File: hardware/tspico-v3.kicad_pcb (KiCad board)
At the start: 4 copper layers, 130 x 64 mm, 157 parts, among them J1 USB-C, J2 microSD, J3 OLED 1.27in 128x96, J4 3.5mm stereo, J5 Joystick, P1 TS2068_Edge, SW1 TS Reset, SW2 NMI, SW3 RUN, SW4 BOOTSEL, U1 74LVC245APW, U10 74LVC257APW, U11 74LVC257APW, U12 74LVC574APW, U13 74LVC574APW, U14 74HC273PW, U15 74LVC541APW, U16 74LVC139PW, U2 74LVC245APW, U20 RP2350B, U21 W25Q128JVSIQ, U22 APS6404L-3SQR-SN, U3 74LVC245APW, U30 TLV1117LV33, U31 TLV1117LV33, U4 74LVC245APW, U40 ESP32-C3-WROOM-02-N4, U5 74LVC04APW, U50 MCP6002, U6 74LVC08APW, U7 74LVC06APW, U8 74LVC126APW, U9 74LVC1G86, Y1 12MHz

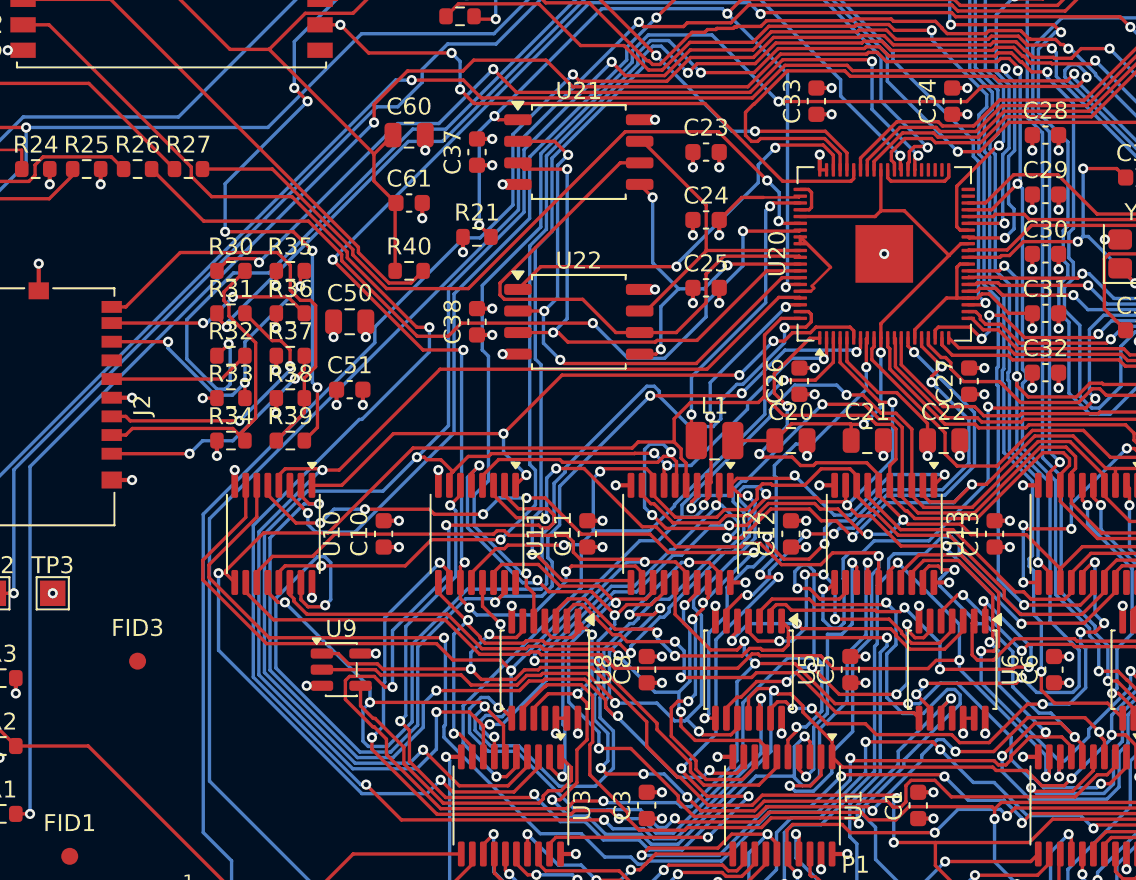
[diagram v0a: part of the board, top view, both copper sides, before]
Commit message: Hand-finish the last eight connections: fully routed, zero DRC errors
finish_route.py adds plane vias, clearance-checked stubs and single-layer
A* routing. Five signals run partly on the +3V3 plane layer (In2). SD_MISO
moves from GP36 to GP32 (both SPI0 RX) because the GP36 pad has no exit.
Schematic, GPIO table and README updated.

Co-Authored-By: Claude Fable 5.1 <noreply@anthropic.com>
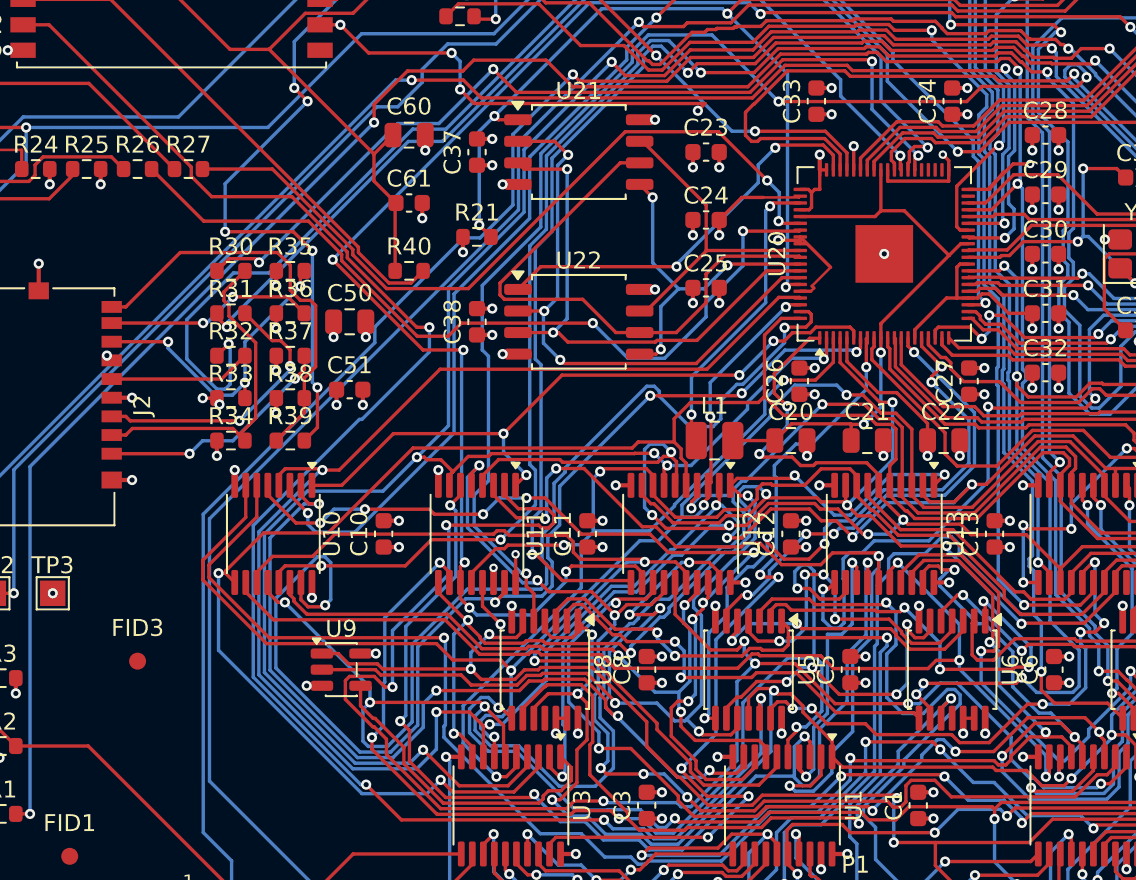
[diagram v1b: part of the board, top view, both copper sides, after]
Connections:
- U20 pad 40: unconnected-(U20-GPIO32-Pad40) -> SD_MISO
- U20 pad 45: SD_MISO -> (no net)
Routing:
- net SD_MISO: track 0.84 -> 64.7 mm, vias 1 -> 3
- net nMWR: track 64.4 -> 90.2 mm
- net MA14: track 19.8 -> 44.8 mm
- net +3V3: track 99.1 -> 105.1 mm, vias 69 -> 72
- net WIFI_TX: track 36.8 -> 37.6 mm, vias 3 -> 5
- net GND: track 123.8 -> 124.2 mm, vias 116 -> 117
- net MA6: track 59.3 -> 59.2 mm, vias 5 -> 6

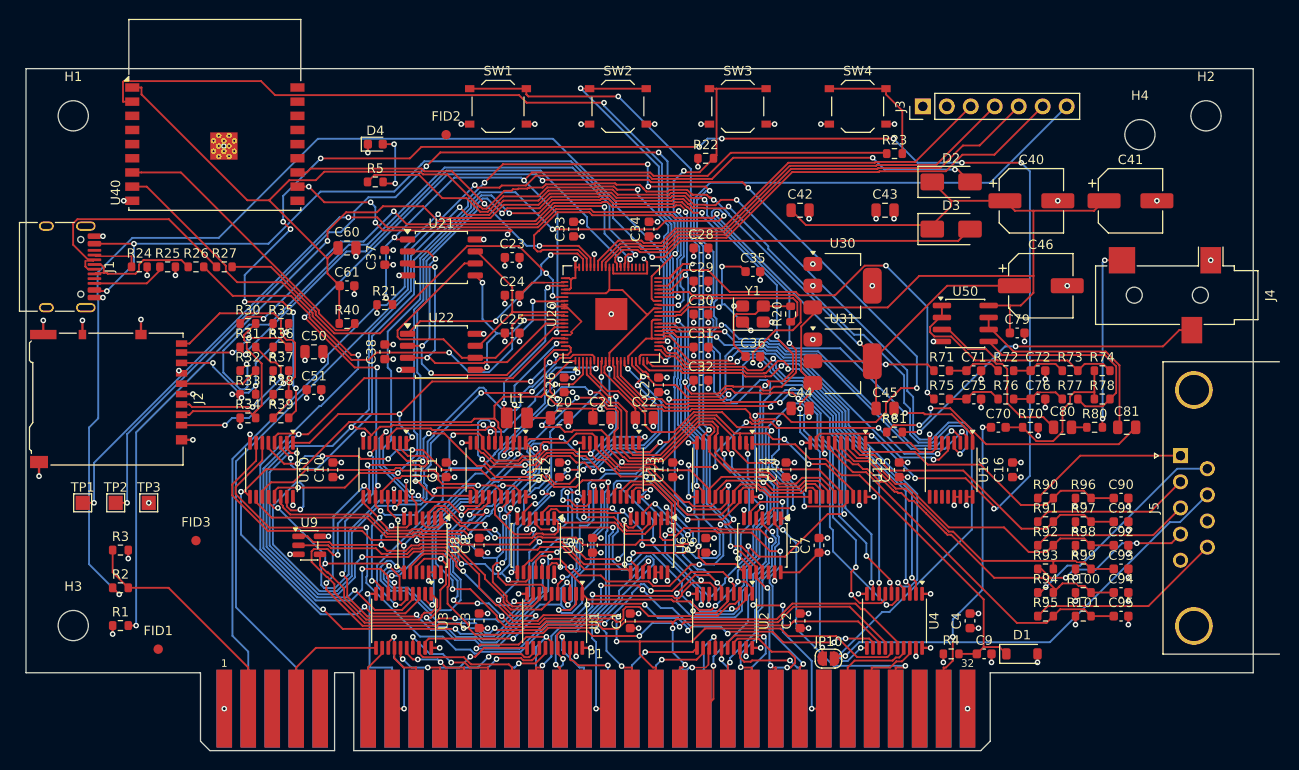
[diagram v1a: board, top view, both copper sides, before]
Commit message: Relayout: 130 x 64.25 mm board with the consolidated logic and cheaper BOM
Regulator and crystal hand-routed per the RP2350 design guide (locked
pre-routes), TF-01A socket flush with the edge, custom footprints from LCSC
land patterns, 0.15 mm signal tracks, 0.6/0.3 vias throughout. New flow:
gen_layout -> preroute -> autoroute -> finish. Zero DRC violations; open are
two nets of the unfitted DMA option (nMRD, nWR_ALO). Fab outputs regenerated.

Co-Authored-By: Claude Fable 5.1 <noreply@anthropic.com>
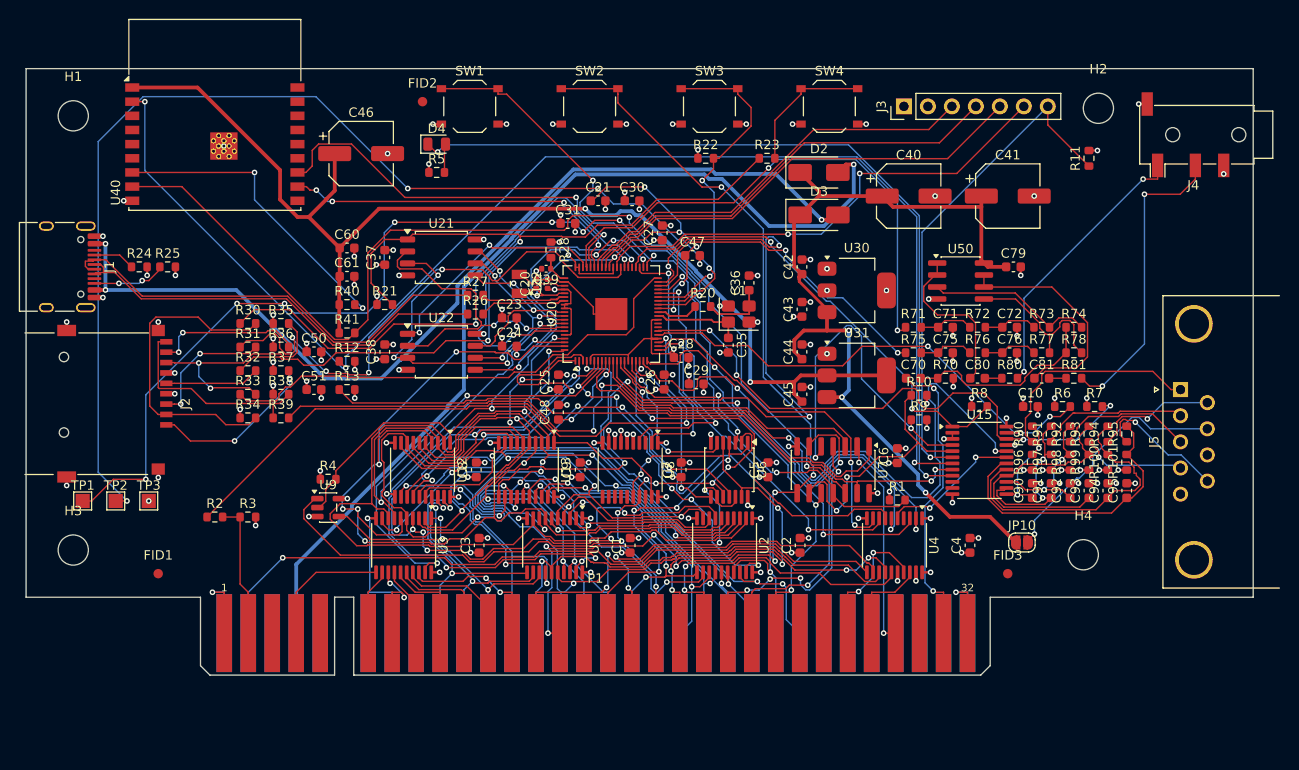
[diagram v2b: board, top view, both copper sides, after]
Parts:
- removed C11, C12, C13, C14, C15, C16, C32, C33, C34: 100n, C_0603_1608Metric
- removed D1: B5819W, D_SOD-123
- removed U10, U11: 74LVC257APW, TSSOP-16_4.4x5mm_P0.65mm
- removed U14: 74HC273PW, TSSOP-20_4.4x6.5mm_P0.65mm
- removed U16: 74LVC139PW, TSSOP-16_4.4x5mm_P0.65mm
- removed U5: 74LVC04APW, TSSOP-14_4.4x5mm_P0.65mm
- added C39: 4.7u, C_0402_1005Metric, F.Cu at (55.1, 21.2)
- added C47: 100n, C_0603_1608Metric, F.Cu at (70.6, 19.8)
- added C48: 100n, C_0603_1608Metric, F.Cu at (56.4, 36.4)
- added R10: 10k, R_0603_1608Metric, F.Cu at (94.6, 34.6)
- added R11: 10k, R_0603_1608Metric, F.Cu at (112.6, 9.50)
- added R12: 10k, R_0603_1608Metric, F.Cu at (34.0, 31.0)
- added R13: 10k, R_0603_1608Metric, F.Cu at (34.0, 34.0)
- added R28: 33, R_0603_1608Metric, F.Cu at (55.6, 19.2)
- added R41: 10k, R_0603_1608Metric, F.Cu at (34.0, 28.0)
- added R6: 4k7, R_0603_1608Metric, F.Cu at (109.8, 35.8)
- added R7: 4k7, R_0603_1608Metric, F.Cu at (113.2, 35.8)
- added R8: 10k, R_0603_1608Metric, F.Cu at (101.0, 35.8)
- added R9: 10k, R_0603_1608Metric, F.Cu at (94.6, 37.2)
- C20, C22: footprint C_0805_2012Metric -> C_0402_1005Metric
- C21: value 4.7u -> 100n; footprint C_0805_2012Metric -> C_0603_1608Metric
- C40, C41, C46: footprint CP_Elec_6.3x5.9 -> CP_Elec_6.3x5.4
- C42, C43, C44, C45, C50, C60, C80, C81: footprint C_0805_2012Metric -> C_0603_1608Metric
- C9: value 1u -> 100n
- D4: footprint LED_0603_1608Metric -> LED_0805_2012Metric
- J2: footprint microSD_HC_Hirose_DM3AT-SF-PEJM5 -> microSD_TF-01A
- J4: footprint Jack_3.5mm_CUI_SJ-3523-SMT_Horizontal -> Jack_3.5mm_PJ320D_Horizontal
- L1: footprint L_1008_2520Metric -> L_Abracon_AOTA-B201610
- R5: value 1k -> 100
- U15: value 74LVC541APW -> XL9555; footprint TSSOP-20_4.4x6.5mm_P0.65mm -> TSSOP-24_4.4x7.8mm_P0.65mm
- U21: value W25Q128JVSIQ -> GD25Q128ESIGR
- U6: value 74LVC08APW -> 74LVC32APW
- U7: value 74LVC06APW -> 74LVC06AD; footprint TSSOP-14_4.4x5mm_P0.65mm -> SOIC-14_3.9x8.7mm_P1.27mm
- U8: value 74LVC126APW -> 74LVC245APW; footprint TSSOP-14_4.4x5mm_P0.65mm -> TSSOP-20_4.4x6.5mm_P0.65mm
- moved FID3 86.1 mm to (104.0, 53.5)
- moved R1 83.4 mm to (92.3, 45.7)
- moved C10 74.2 mm to (106.4, 35.8), turned to 0 degrees
- moved C46 73.3 mm to (35.5, 9.00)
- moved R4 68.5 mm to (32.0, 43.5)
- moved C9 47.0 mm to (58.7, 42.5), turned to 90 degrees
- moved H4 44.9 mm to (112.0, 51.5)
- moved R26 30.0 mm to (47.6, 26.0)
- moved R27 26.8 mm to (47.6, 24.0)
- moved JP10 23.9 mm to (105.5, 50.2)
- moved U8 23.4 mm to (64.0, 42.5)
- moved C21 23.0 mm to (60.6, 14.0)
- moved C6 22.4 mm to (92.3, 41.0)
- moved R95 21.1 mm to (116.6, 38.7), turned to 90 degrees
- moved C5 20.2 mm to (78.6, 42.5)
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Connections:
- net /Local Bus and Registers/LED_K renamed /Local Bus and Registers/LED_A
- C9 pad 1: /Local Bus and Registers/nPOR -> +3V3
- D4 pad 1: GND -> /Local Bus and Registers/nLED
- P1 pad A25: /2068 Interface/nM1 -> unconnected-(P1-~{M1}-PadA25)
- P1 pad A26: /2068 Interface/nRFSH -> unconnected-(P1-~{RFSH}-PadA26)
- R4 pad 2: /Local Bus and Registers/nPOR -> nDMA_EN
- R5 pad 1: LED -> +3V3
- U1 pad 1: DMA_EN -> GND
- U1 pad 19: GND -> nAEN_X
- U1 pad 2: MA12 -> MD4
- U1 pad 3: MA13 -> MD5
- U1 pad 4: MA14 -> MD6
- U1 pad 5: MA15 -> MD7
- U1 pad 6: MA3 -> MD3
- U1 pad 7: MA2 -> MD2
- U1 pad 8: MA1 -> MD1
- U1 pad 9: MA0 -> MD0
- U12 pad 11: /Local Bus and Registers/nWR_ALO -> nWR_ALO
- U12 pad 12: MA7 -> /2068 Interface/A7
- U12 pad 13: MA6 -> /2068 Interface/A6
- U12 pad 14: MA5 -> /2068 Interface/A5
- U12 pad 15: MA4 -> /2068 Interface/A4
- U12 pad 16: MA3 -> /2068 Interface/A3
- U12 pad 17: MA2 -> /2068 Interface/A2
- U12 pad 18: MA1 -> /2068 Interface/A1
- U12 pad 19: MA0 -> /2068 Interface/A0
- U13 pad 11: /Local Bus and Registers/nWR_AHI -> nWR_AHI
- U13 pad 12: MA15 -> /2068 Interface/A15
- U13 pad 13: MA14 -> /2068 Interface/A14
- U13 pad 14: MA13 -> /2068 Interface/A13
- U13 pad 15: MA12 -> /2068 Interface/A12
- U13 pad 16: MA11 -> /2068 Interface/A11
- U13 pad 17: MA10 -> /2068 Interface/A10
- U13 pad 18: MA9 -> /2068 Interface/A9
- U13 pad 19: MA8 -> /2068 Interface/A8
- U15 pad 1: /Local Bus and Registers/nRD_STAT -> nIOX_INT
- U15 pad 10: GND -> unconnected-(U15-IO0_6-Pad10)
- U15 pad 11: MD7 -> unconnected-(U15-IO0_7-Pad11)
- U15 pad 12: MD6 -> GND
- U15 pad 13: MD5 -> JOY_UP
- U15 pad 14: MD4 -> JOY_DOWN
- U15 pad 15: MD3 -> JOY_LEFT
- U15 pad 16: MD2 -> JOY_RIGHT
- U15 pad 17: MD1 -> JOY_FIRE1
- U15 pad 18: MD0 -> JOY_FIRE2
- U15 pad 19: GND -> nBUSAK_L
- U15 pad 2: JOY_UP -> GND
- U15 pad 20: +3V3 -> SD_CD
- U15 pad 3: JOY_DOWN -> GND
- U15 pad 4: JOY_LEFT -> BUSRQ
- U15 pad 5: JOY_RIGHT -> NMI_REQ
- U15 pad 6: JOY_FIRE1 -> nOLED_RST
- U15 pad 7: JOY_FIRE2 -> WIFI_EN
- U15 pad 8: nBUSAK -> WIFI_DL
- U15 pad 9: SD_CD -> /Local Bus and Registers/nLED
- U2 pad 1: DMA_EN -> GND
- U2 pad 19: GND -> nAEN_Y
- U2 pad 2: MA4 -> MD0
- U2 pad 3: MA5 -> MD1
- U2 pad 4: MA6 -> MD2
- U2 pad 5: MA7 -> MD3
- U2 pad 6: MA8 -> MD4
- U2 pad 7: MA9 -> MD5
- U2 pad 8: MA10 -> MD6
- U2 pad 9: MA11 -> MD7
- U20 pad 14: nMREQ_V -> nMEMRD
- U20 pad 16: nIORQ_V -> nMEMWR
- U20 pad 17: nRD_L -> nIORD
- U20 pad 18: nWR_L -> nIOWR
- U20 pad 25: REG_SEL0 -> I2C_SDA
- U20 pad 26: REG_SEL1 -> I2C_SCL
- U20 pad 27: nREG_STB -> nWR_ALO
- U20 pad 39: unconnected-(U20-GPIO31-Pad39) -> nWR_AHI
- U20 pad 42: unconnected-(U20-GPIO33-Pad42) -> nDMA_EN
- U20 pad 43: unconnected-(U20-GPIO34-Pad43) -> nDMA_MREQ
- U20 pad 44: unconnected-(U20-GPIO35-Pad44) -> nIOX_INT
- U20 pad 45: (no net) -> unconnected-(U20-GPIO36-Pad45)
- U20 pad 6: ASEL -> nAEN_X
- U20 pad 61: +3V3 -> /RP2350B Core/VREG_AVDD
- U20 pad 7: nAOE -> nAEN_Y
- U4 pad 15: /2068 Interface/nRD -> nBUSAK
- U4 pad 16: /2068 Interface/nWR -> GND
- U4 pad 4: nWR_L -> unconnected-(U4-A2-Pad4)
- U4 pad 5: nRD_L -> nBUSAK_L
- U6 pad 1: /2068 Interface/MREQ_H -> /2068 Interface/nMREQ
- U6 pad 10: nMWR -> /2068 Interface/nRD
- U6 pad 11: unconnected-(U6-Pad11) -> nIOWR
- U6 pad 12: GND -> /2068 Interface/nIORQ
- U6 pad 13: GND -> /2068 Interface/nWR
- U6 pad 2: /2068 Interface/nRFSH -> /2068 Interface/nRD
- U6 pad 3: /2068 Interface/MREQ_RFSH -> nMEMRD
- U6 pad 4: /2068 Interface/IORQ_H -> /2068 Interface/nMREQ
- U6 pad 5: /2068 Interface/nM1 -> /2068 Interface/nWR
- U6 pad 6: /2068 Interface/IORQ_M1 -> nMEMWR
- U6 pad 8: /2068 Interface/nDMA_MREQ -> nIORD
- U6 pad 9: nMRD -> /2068 Interface/nIORQ
- U7 pad 12: unconnected-(U7-Pad12) -> nWIFI_BOOT
- U7 pad 13: GND -> WIFI_DL
- U8 pad 1: DMA_EN -> +3V3
- U8 pad 10: DMA_EN -> GND
- U8 pad 12: GND -> unconnected-(U8-B6-Pad12)
- U8 pad 13: GND -> unconnected-(U8-B5-Pad13)
- U8 pad 14: +3V3 -> unconnected-(U8-B4-Pad14)
- U8 pad 2: /2068 Interface/nDMA_MREQ -> nDMA_MREQ
- U8 pad 3: /2068 Interface/nMREQ -> nMRD
- U8 pad 4: DMA_EN -> nMWR
- U8 pad 5: nMRD -> GND
- U8 pad 6: /2068 Interface/nRD -> GND
- U8 pad 8: /2068 Interface/nWR -> GND
- U8 pad 9: nMWR -> GND
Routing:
- net MA7: track 173.3 -> 0.00 mm, vias 10 -> 0
- net MA10: track 165.3 -> 0.00 mm, vias 8 -> 0
- net MA8: track 160.6 -> 0.00 mm, vias 8 -> 0
- net nMRD: track 146.5 -> 0.00 mm, vias 9 -> 0
- net /Local Bus and Registers/nWR_ALO: track 112.2 -> 0.00 mm, vias 4 -> 0
- net MA4: track 96.6 -> 0.00 mm, vias 7 -> 0
- net MD5: track 193.0 -> 96.6 mm, vias 10 -> 8
- net /2068 Interface/SPKR_TAPE: track 170.5 -> 75.0 mm, vias 3 -> 1
- net RESET_HOLD: track 138.3 -> 44.5 mm, vias 5 -> 2
- net MA9: track 89.4 -> 0.00 mm, vias 4 -> 0
- net nWR_AHI: track 0.00 -> 87.4 mm, vias 0 -> 5
- net /Local Bus and Registers/nLED: track 0.00 -> 86.5 mm, vias 0 -> 2
- net DMA_EN: track 86.0 -> 0.00 mm, vias 7 -> 0
- net LED: track 73.3 -> 0.00 mm, vias 2 -> 0
- net nAOE: track 68.5 -> 0.00 mm, vias 5 -> 0
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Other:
- board size 130 x 64 mm -> 130 x 56 mm

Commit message: Drop the DMA option: board fully routed, zero DRC errors
DMA_OPTION = False removes U8, U9, U12, U13 and six GPIOs; the data transceiver
takes DIR from /RD with its A side on the Z80 bus. Rerouted with the scripted
flow; finish order is DVDD before +3V3, supply pin 29 escapes through the freed
pad lanes, DVDD widened to 0.25 mm. No signal on either plane layer, all vias
0.6/0.3. Fab outputs regenerated; parts + fees $14.48 per board at 10 boards.

Co-Authored-By: Claude Fable 5.1 <noreply@anthropic.com>
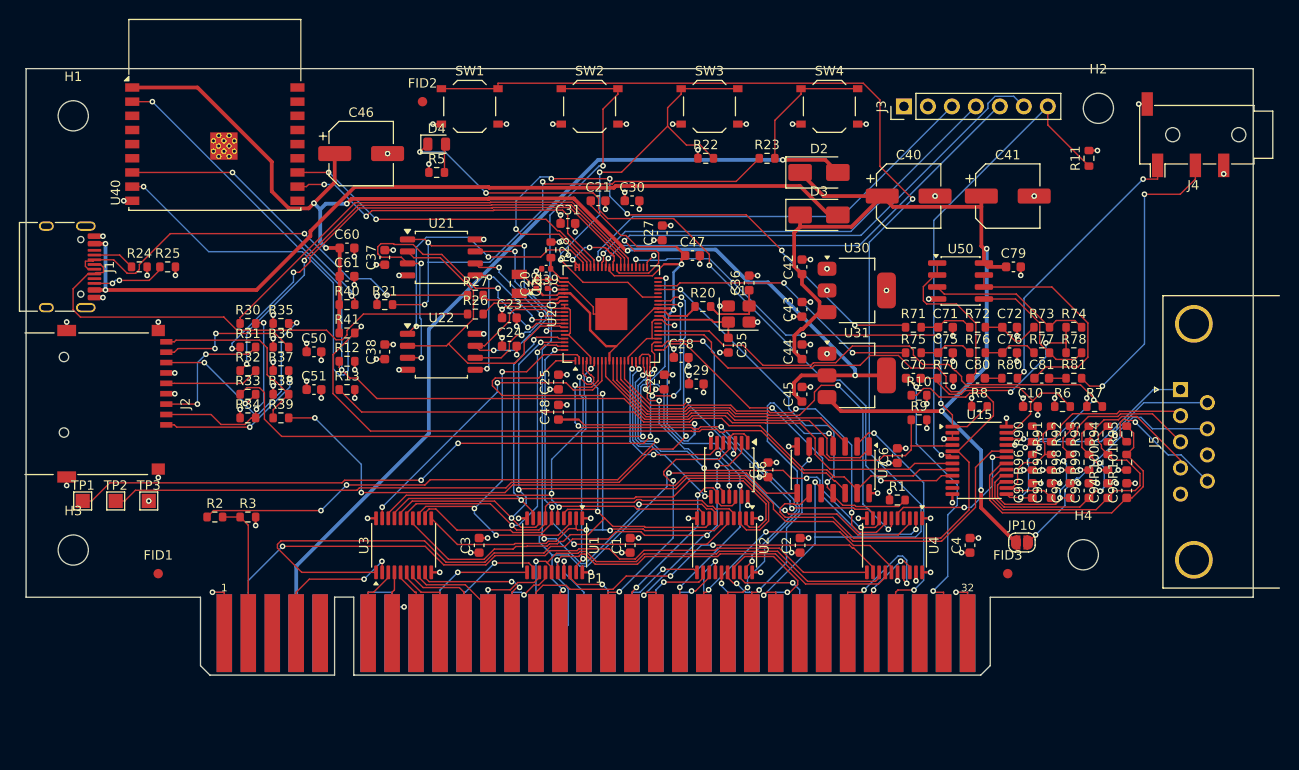
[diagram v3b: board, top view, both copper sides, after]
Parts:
- removed C7, C8, C9: 100n, C_0603_1608Metric
- removed R4: 10k, R_0603_1608Metric
- removed U12, U13: 74LVC574APW, TSSOP-20_4.4x6.5mm_P0.65mm
- removed U8: 74LVC245APW, TSSOP-20_4.4x6.5mm_P0.65mm
- removed U9: 74LVC1G86, SOT-23-5
- turned U3 to 90 degrees
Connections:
- U20 pad 27: nWR_ALO -> unconnected-(U20-GPIO26-Pad27)
- U20 pad 28: nMRD -> unconnected-(U20-GPIO27-Pad28)
- U20 pad 36: nMWR -> unconnected-(U20-GPIO28-Pad36)
- U20 pad 39: nWR_AHI -> unconnected-(U20-GPIO31-Pad39)
- U20 pad 42: nDMA_EN -> unconnected-(U20-GPIO33-Pad42)
- U20 pad 43: nDMA_MREQ -> unconnected-(U20-GPIO34-Pad43)
- U3 pad 1: /2068 Interface/DATA_DIR -> /2068 Interface/nRD
- U3 pad 11: /2068 Interface/D7 -> MD4
- U3 pad 12: /2068 Interface/D0 -> MD3
- U3 pad 13: /2068 Interface/D1 -> MD5
- U3 pad 14: /2068 Interface/D2 -> MD6
- U3 pad 15: /2068 Interface/D6 -> MD2
- U3 pad 16: /2068 Interface/D5 -> MD1
- U3 pad 17: /2068 Interface/D3 -> MD0
- U3 pad 18: /2068 Interface/D4 -> MD7
- U3 pad 2: MD4 -> /2068 Interface/D7
- U3 pad 3: MD3 -> /2068 Interface/D0
- U3 pad 4: MD5 -> /2068 Interface/D1
- U3 pad 5: MD6 -> /2068 Interface/D2
- U3 pad 6: MD2 -> /2068 Interface/D6
- U3 pad 7: MD1 -> /2068 Interface/D5
- U3 pad 8: MD0 -> /2068 Interface/D3
- U3 pad 9: MD7 -> /2068 Interface/D4
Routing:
- net nWR_AHI: track 87.4 -> 0.00 mm, vias 5 -> 0
- net nDMA_EN: track 82.8 -> 0.00 mm, vias 4 -> 0
- net /2068 Interface/A5: track 74.5 -> 16.2 mm, vias 4 -> 1
- net MD2: track 111.9 -> 63.4 mm, vias 6 -> 2
- net /2068 Interface/nRESET: track 86.0 -> 132.0 mm
- net MD6: track 104.0 -> 58.5 mm, vias 4 -> 2
- net /2068 Interface/A4: track 56.4 -> 12.0 mm, vias 3 -> 1
- net /2068 Interface/A7: track 50.4 -> 6.72 mm, vias 3 -> 1
- net /2068 Interface/A6: track 50.3 -> 8.08 mm, vias 2 -> 1
- net /RP2350B Core/SWDIO: track 123.2 -> 81.0 mm, vias 4 -> 2
- net nAEN_X: track 59.6 -> 23.5 mm, vias 4 -> 2
- net MD1: track 108.5 -> 75.0 mm, vias 8 -> 3
- net WIFI_EN: track 142.8 -> 110.8 mm, vias 3 -> 2
- net MD0: track 100.6 -> 71.5 mm
- net MD5: track 96.6 -> 68.1 mm, vias 8 -> 5
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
